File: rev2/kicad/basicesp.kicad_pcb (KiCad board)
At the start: 2 copper layers, 47 x 49.5 mm, 17 parts, among them P1 CONN_01X02, P2 CONN_01X02, P3 CONN_01X08, P4 CONN_01X08, P5 CONN_01X10, P6 CONN_01X05, SW1 SW_PUSH_SMALL_H, U1 LM1117-3.3

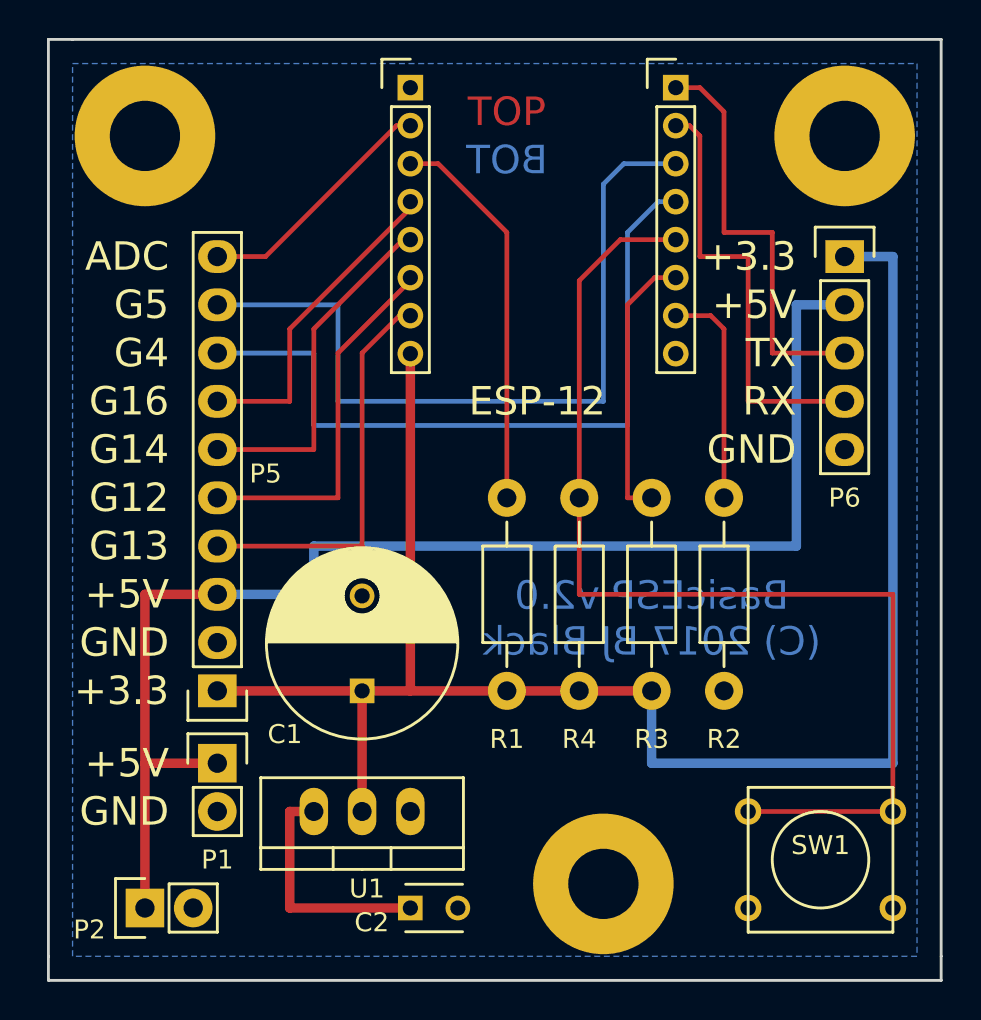
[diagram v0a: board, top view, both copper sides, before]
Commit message: Update to revision B (fix two disconnected nodes).
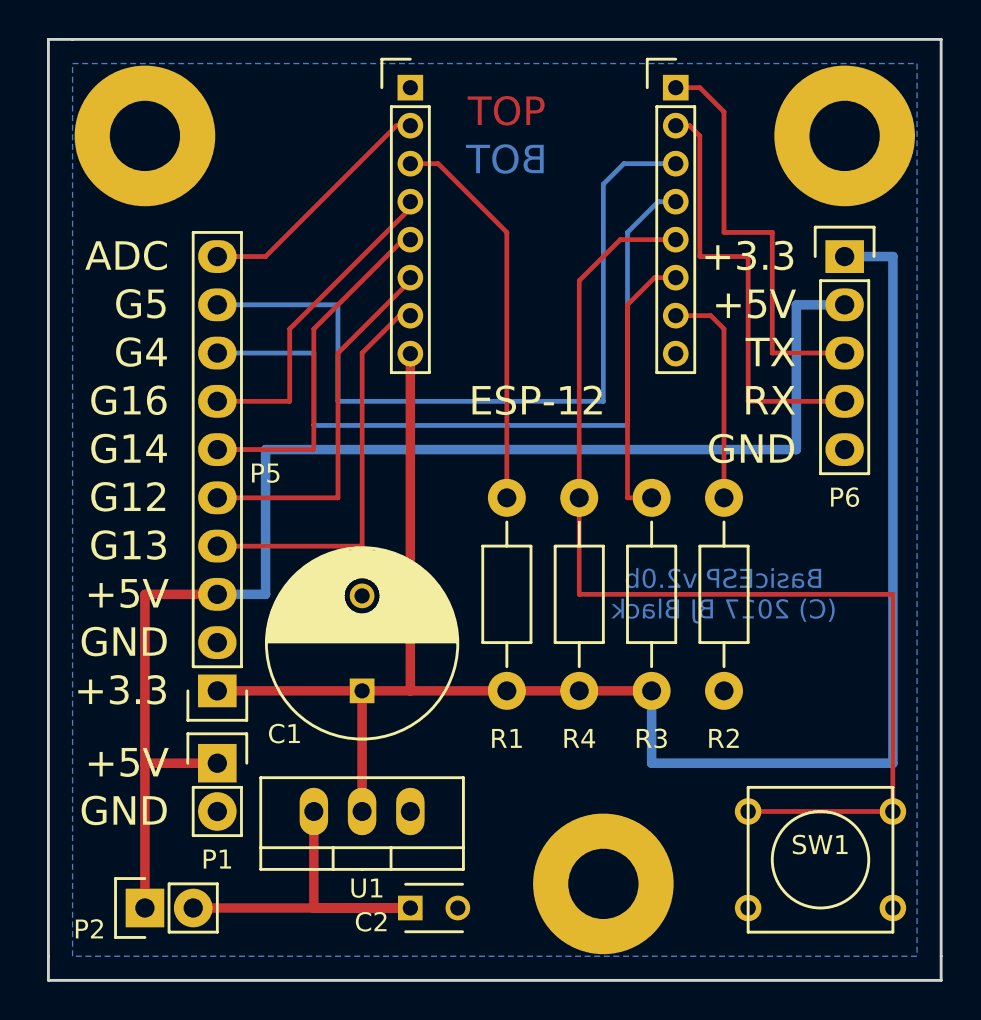
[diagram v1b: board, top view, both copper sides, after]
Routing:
- net Net-(C2-Pad1): track 12.7 -> 21.6 mm
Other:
- board text added: "BasicESP v2.0b (C) 2017 BJ Black"
- board text removed: "BasicESP v2.0 (C) 2017 BJ Black"
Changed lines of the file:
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@@
   (general
     (links 36)
-    (no_connects 3)
-    (area 74.854999 54.534999 121.995001 104.215001)
+    (no_connects 1)
+    (area 59.460001 51.175 126.754286 111.920001)
     (thickness 1.6)
     (drawings 30)
@@
     (35 F.Paste user)
     (36 B.SilkS user)
-    (37 F.SilkS user)
+    (37 F.SilkS user hide)
     (38 B.Mask user)
     (39 F.Mask user)
@@
     (visible_elements FFFEFF7F)
     (pcbplotparams
-      (layerselection 0x00030_80000001)
+      (layerselection 0x010e0_80000001)
       (usegerberextensions false)
       (excludeedgelayer true)
@@
       (outputformat 1)
       (mirror false)
-      (drillshape 1)
+      (drillshape 0)
       (scaleselection 1)
-      (outputdirectory ""))
+      (outputdirectory basicesp.wjblack.com.rev.2.0b/))
   )
   (net 0 "")
@@
     (arrow2b (pts (xy 67.31 54.61) (xy 67.896421 55.736504)))
   )
-  (gr_text "BasicESP v2.0\n(C) 2017 BJ Black" (at 106.68 85.09) (layer B.Cu)
-    (effects (font (size 1.5 1.5) (thickness 0.3)) (justify mirror))
+  (gr_text "BasicESP v2.0b\n(C) 2017 BJ Black" (at 110.49 83.82) (layer B.Cu)
+    (effects (font (size 1 1) (thickness 0.25)) (justify mirror))
   )
   (gr_text GND (at 81.28 95.25) (layer F.SilkS)
@@
   (segment (start 93.98 88.9) (end 99.06 88.9) (width 0.5) (layer F.Cu) (net 1))
   (segment (start 83.82 88.9) (end 91.44 88.9) (width 0.5) (layer F.Cu) (net 1))
-  (segment (start 88.9 95.25) (end 87.63 95.25) (width 0.5) (layer F.Cu) (net 3))
-  (segment (start 87.63 95.25) (end 87.63 100.33) (width 0.5) (layer F.Cu) (net 3))
-  (segment (start 93.98 100.33) (end 87.63 100.33) (width 0.5) (layer F.Cu) (net 3))
+  (segment (start 93.98 100.33) (end 82.55 100.33) (width 0.5) (layer F.Cu) (net 3))
+  (segment (start 88.9 95.25) (end 88.9 100.33) (width 0.5) (layer F.Cu) (net 3))
+  (segment (start 88.9 100.33) (end 93.98 100.33) (width 0.5) (layer F.Cu) (net 3))
+  (segment (start 83.82 83.82) (end 86.36 83.82) (width 0.5) (layer B.Cu) (net 4))
+  (segment (start 114.3 68.58) (end 116.84 68.58) (width 0.5) (layer B.Cu) (net 4))
+  (segment (start 114.3 76.2) (end 114.3 68.58) (width 0.5) (layer B.Cu) (net 4))
+  (segment (start 86.36 76.2) (end 114.3 76.2) (width 0.5) (layer B.Cu) (net 4))
+  (segment (start 86.36 83.82) (end 86.36 76.2) (width 0.5) (layer B.Cu) (net 4))
   (segment (start 80.01 92.71) (end 83.82 92.71) (width 0.5) (layer F.Cu) (net 4))
   (segment (start 83.82 83.82) (end 80.01 83.82) (width 0.5) (layer F.Cu) (net 4))
   (segment (start 80.01 83.82) (end 80.01 92.71) (width 0.5) (layer F.Cu) (net 4))
   (segment (start 80.01 92.71) (end 80.01 100.33) (width 0.5) (layer F.Cu) (net 4))
-  (segment (start 83.82 83.82) (end 88.9 83.82) (width 0.5) (layer B.Cu) (net 4))
-  (segment (start 114.3 68.58) (end 116.84 68.58) (width 0.5) (layer B.Cu) (net 4))
-  (segment (start 114.3 81.28) (end 114.3 68.58) (width 0.5) (layer B.Cu) (net 4))
-  (segment (start 88.9 81.28) (end 114.3 81.28) (width 0.5) (layer B.Cu) (net 4))
-  (segment (start 88.9 83.82) (end 88.9 81.28) (width 0.5) (layer B.Cu) (net 4))
   (segment (start 83.82 66.04) (end 86.36 66.04) (width 0.25) (layer F.Cu) (net 6))
   (segment (start 93.25 59.15) (end 93.98 59.15) (width 0.25) (layer F.Cu) (net 6))
